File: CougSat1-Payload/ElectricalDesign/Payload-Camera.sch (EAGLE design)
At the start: 0 parts

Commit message: Added ADC
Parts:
- added C1: 4.7µF 10%, CougsInSpace-Capacitors:CAP-POL-V-4.7UF-4028
- added C2, C6, C7, C9: 100nF 10%, CougsInSpace-Capacitors:CAP-V-100NF-1608
- added C3: 10µF 10%, CougsInSpace-Capacitors:CAP-V-10UF-1608
- added C4, C5: 1µF 10%, CougsInSpace-Capacitors:CAP-V-1UF-1608
- added FB1: 1.5kΩ @ 100MHz, CougsInSpace-Coils:CHOKE-H-1.5K-1608
- added J1: CougSat Card, CougsInSpace-Boards:CIS_CARD
- added Q1: MMBTA06W, CougsInSpace-DiscreteSemi:BJT-NPN-MMBTA06W-SOT323
- added RN1: 10kΩ 5%, CougsInSpace-Resistors:RES_BUS-10-10K-3264
- added RT1, RT2, RT3, RT4, RT5, RT6, RT7, RT8: 10kΩ 5%, CougsInSpace-Resistors:THERMISTOR-V-10K-1608
- added TP1, TP2, TP3: TEST_POINT-SMD-C-1.25, CougsInSpace-Connectors:TEST_POINT-SMD-C-1.25
- added U1: AD7291, CougsInSpace-IC-Conversion:AD7291
- added U2: AD8515, CougsInSpace-IC-Amplifiers:OPAMP-1-AD8515
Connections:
- new net 3.3V_10: C9.1, FB1.1, J1POWER.PR_3.3V-10, U1.!PD!/!RST, U1.VDRIVE
- new net 3.3V_11: J1POWER.PR_3.3V-11
- new net 3.3V_12: J1POWER.PR_3.3V-12
- new net AGND: C1.C, C2.2, C3.2, C6.2, C7.2, U1.AGND, U2.V-
- new net AVDD: C1.A, C2.1, C6.1, C7.1, FB1.2, Q1.C, TP1.1, U1.VDD, U2.V+
- new net AVREF-0: C5.1, Q1.E, RN1.C, TP3.1, U2.IN-
- new net CHASSIS: J1POWER.CHASSIS
- new net DGND: C4.2, C5.2, C9.2, RT1.1, RT2.1, RT3.1, RT4.1, RT5.1, RT6.1, RT7.1, RT8.1, U1.DGND
- new net I2C_SCL: J1DATA.BUS_I2C1_SCL, U1.SCL
- new net I2C_SDA: J1DATA.BUS_I2C1_SDA, U1.SDA
- new net N$10: RN1.1, RT1.2, U1.IN7
- new net N$14: RN1.8, RT6.2, U1.IN0
- new net N$16: RN1.6, RT8.2, U1.IN2
- new net N$2: C3.1, TP2.1, U1.VREF, U2.IN+
- new net N$3: C4.1, U1.DCAP
- new net N$4: RN1.7, RT7.2, U1.IN1
- new net N$5: Q1.B, U2.OUT
- new net N$6: RN1.5, RT5.2, U1.IN3
- new net N$7: RN1.4, RT2.2, U1.IN4
- new net N$8: RN1.3, RT3.2, U1.IN5
- new net N$9: RN1.2, RT4.2, U1.IN6
- new net PGND: J1POWER.PGND
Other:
- note added: "CAD Note: Decoupling"
- note added: "Connector: Backplane"
- note added: "Page 1: Block Diagram Page 2: Power Rails Page 3: Schematic Page 4: Mechanical"
- note removed: "Connector: Backplane From EPS"
- note removed: "Connector: To Backplane"
- note removed: "Page 1: Block Diagram Page 2: Power Rails"

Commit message: Added cameras
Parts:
- removed Q1: MMBTA06W, CougsInSpace-DiscreteSemi:BJT-NPN-MMBTA06W-SOT323
- added B1, B2: ArduCam OV5642, CougsInSpace-Sensors:ARDUCAM-5MP-1.7MM-F2.8
- added D1: X100-7, CougsInSpace-Sensors:PHOTODIODE-X100-7-THD
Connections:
- net N$2 renamed ADC_VREF
- net N$3 renamed ADC_DCAP
- removed net N$5: Q1.B, U2.OUT
- new net !CS-TELEPHOTO: B1.!CS
- new net !CS-WIDE_ANGLE: B2.!CS
- new net SPI_MISO: B1.MISO, B2.MISO, J1DATA.BUS_SPI_MISO
- new net SPI_MOSI: B1.MOSI, B2.MOSI, J1DATA.BUS_SPI_MOSI
- new net SPI_SCK: B1.SCK, B2.SCK, J1DATA.BUS_SPI_SCK
- net 3.3V_11: now also B1.VCC
- net 3.3V_12: now also B2.VCC
- net AVDD: no longer Q1.C
- net AVREF-0: now also U2.OUT; no longer Q1.E
- net CHASSIS: now also B1.CHASSIS, B2.CHASSIS
- net DGND: now also B1.DGND, B2.DGND
- net I2C_SCL: now also B1.SCL, B2.SCL
- net I2C_SDA: now also B1.SDA, B2.SDA
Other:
- note added: "Page 1: Block Diagram Page 2: Power Rails Page 3: Connector/ADC/Cameras Page 4: Geiger Counter Page 4: Mechanical"
- note removed: "Page 1: Block Diagram Page 2: Power Rails Page 3: Schematic Page 4: Mechanical"

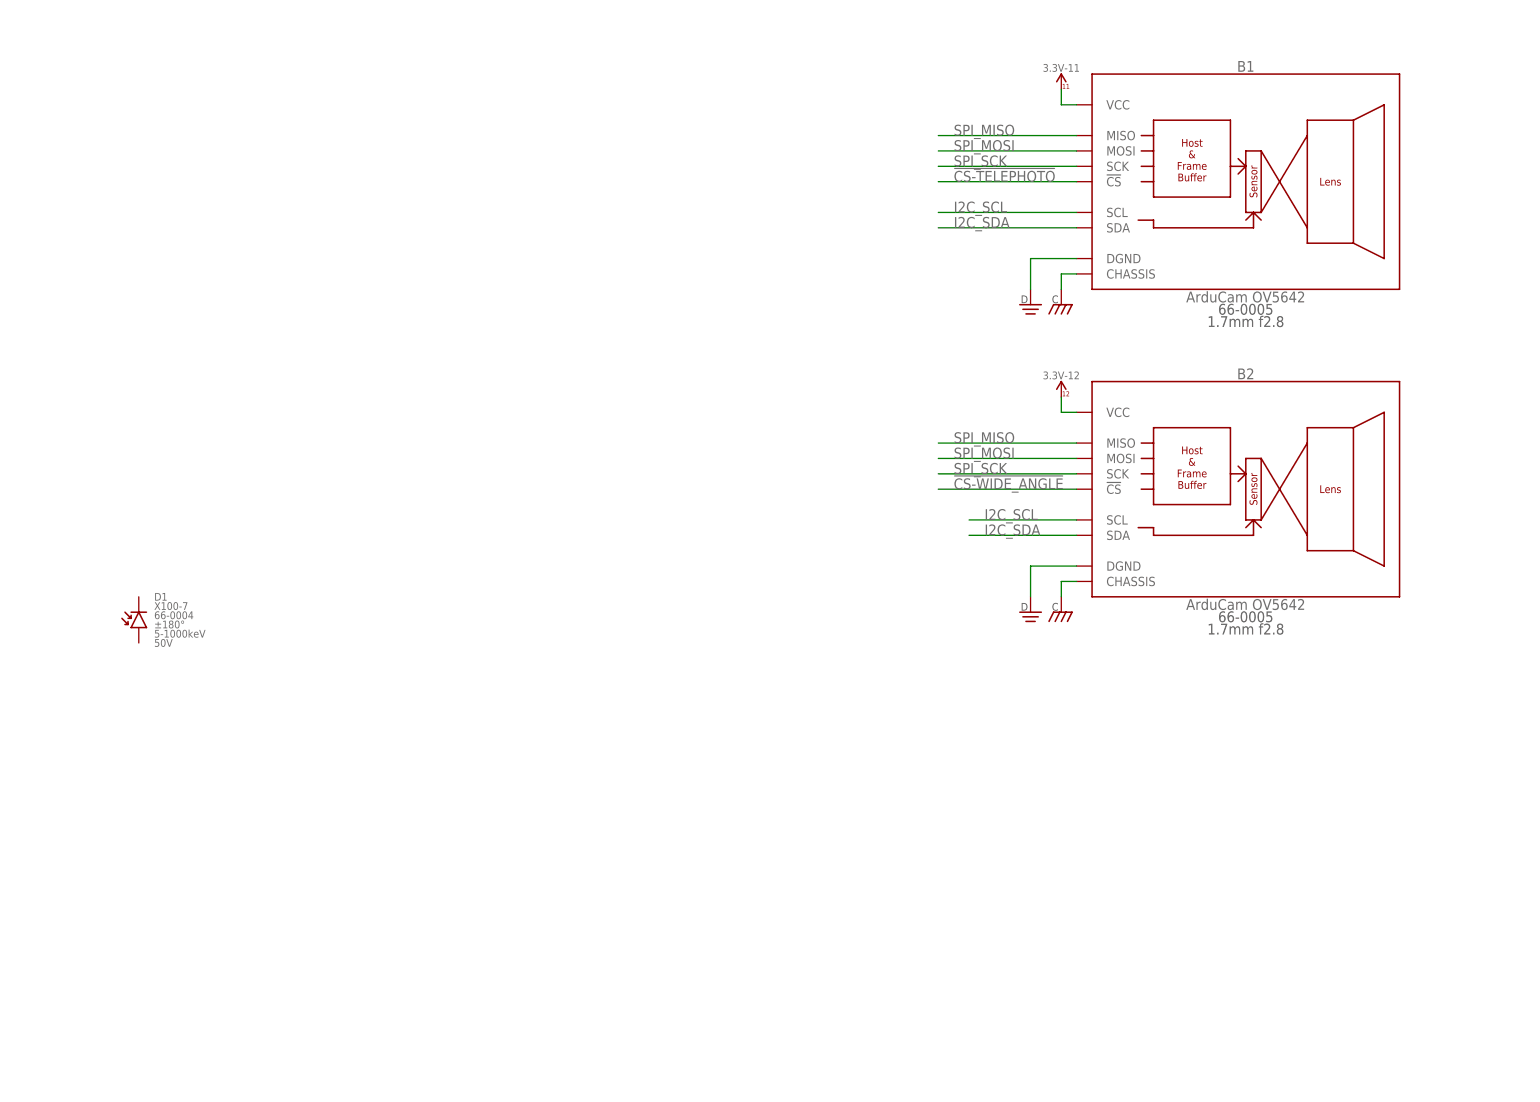
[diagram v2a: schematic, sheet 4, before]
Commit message: Added geiger counter
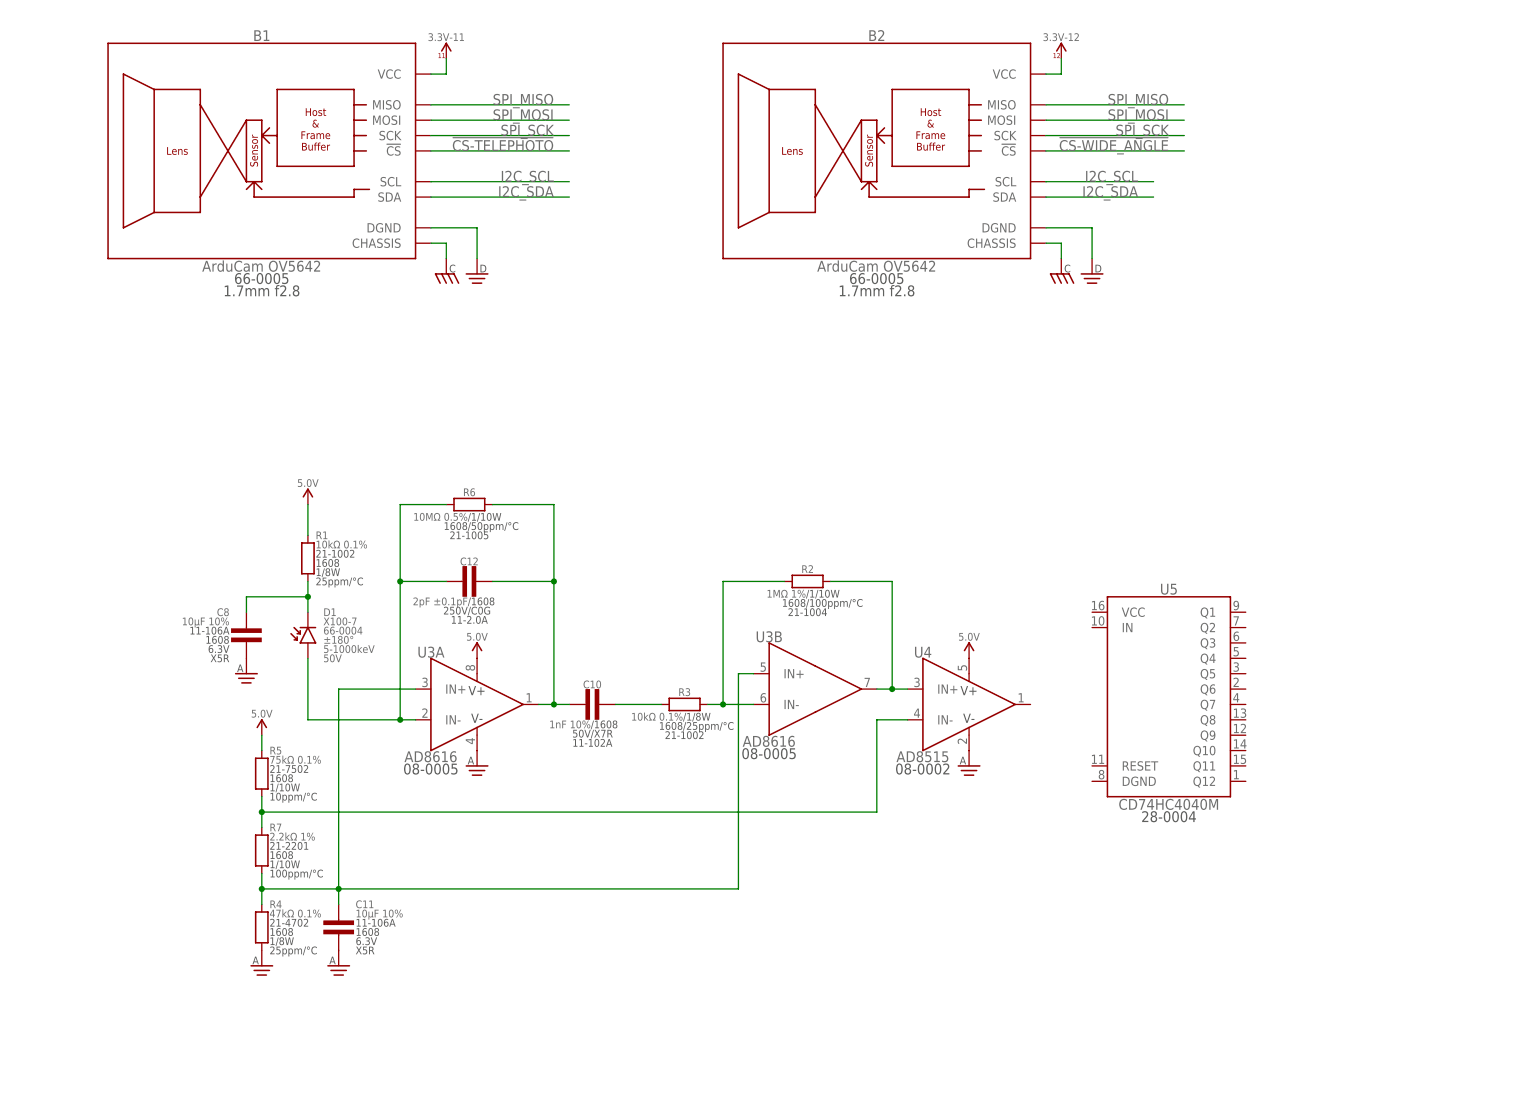
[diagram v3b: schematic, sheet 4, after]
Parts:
- added C10: 1nF 10%, CougsInSpace-Capacitors:CAP-H-1NF-1608
- added C11, C8: 10µF 10%, CougsInSpace-Capacitors:CAP-V-10UF-1608
- added C12: 2pF ±0.1pF, CougsInSpace-Capacitors:CAP-H-2PF-1608
- added R1: 10kΩ 0.1%, CougsInSpace-Resistors:RES-V-10K-1608
- added R2: 1MΩ 1%, CougsInSpace-Resistors:RES-H-1M-1608
- added R3: 10kΩ 0.1%, CougsInSpace-Resistors:RES-H-10K-1608
- added R4: 47kΩ 0.1%, CougsInSpace-Resistors:RES-V-47K-1608
- added R5: 75kΩ 0.1%, CougsInSpace-Resistors:RES-V-75K-1608
- added R6: 10MΩ 0.5%, CougsInSpace-Resistors:RES-H-10M-1608
- added R7: 2.2kΩ 1%, CougsInSpace-Resistors:RES-V-2.2K-1608
- added U3: AD8616, CougsInSpace-IC-Amplifiers:OPAMP-2-AD8616-MSOP8
- added U4: AD8515, CougsInSpace-IC-Amplifiers:OPAMP-1-AD8515
- added U5: CD74HC4040M, CougsInSpace-IC-Logic:COUNTER_BINARY-12BITSO16
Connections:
- new net 5.0V: R1.2, R5.2, U3A.V+, U4.V+
- new net N$1: C8.1, D1.C, R1.1
- new net N$11: C11.1, R4.2, R7.1, U3A.IN+, U3B.IN+
- new net N$12: C10.2, R3.1
- new net N$13: R2.1, R3.2, U3B.IN-
- new net N$15: R2.2, U3B.OUT, U4.IN+
- new net N$2: C12.1, D1.A, R6.1, U3A.IN-
- new net N$3: R5.1, R7.2, U4.IN-
- new net N$5: C10.1, C12.2, R6.2, U3A.OUT
- net AGND: now also C11.2, C8.2, R4.1, U3A.V-, U4.V-
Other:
- moved on the sheet: B1, B2, D1

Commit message: Created design document
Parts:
- added C13: 10nF 10%, CougsInSpace-Capacitors:CAP-V-10NF-1608
- added C14, C15: 10µF 10%, CougsInSpace-Capacitors:CAP-V-10UF-1608
- added U6: TPS73250, CougsInSpace-IC-Power:LDO-FB-5.0-SOT23-5
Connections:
- new net N$17: U4.OUT, U5.IN
- new net N$18: U6.EN, U6.IN
- new net N$19: C13.1, U6.FB
- net 3.3V_10: now also U5.VCC
- net 5.0V: now also C14.1, U6.OUT
- net DGND: now also U5.DGND
- net PGND: now also C13.2, C14.2, U6.PGND
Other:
- note added: "3xx>"
- note added: "3xx> 4xx>"
- note added: "4xx>"
- note added: "4xx> 4xx>"
- note added: "<3xx"
- note added: "<3xx>"
- note added: "<3xx> <4xx>"
- note added: "<4xx <4xx"
- moved on the sheet: C10, C11, C12, C3, C4, C5, C6, C7, C8, C9, D1, R1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

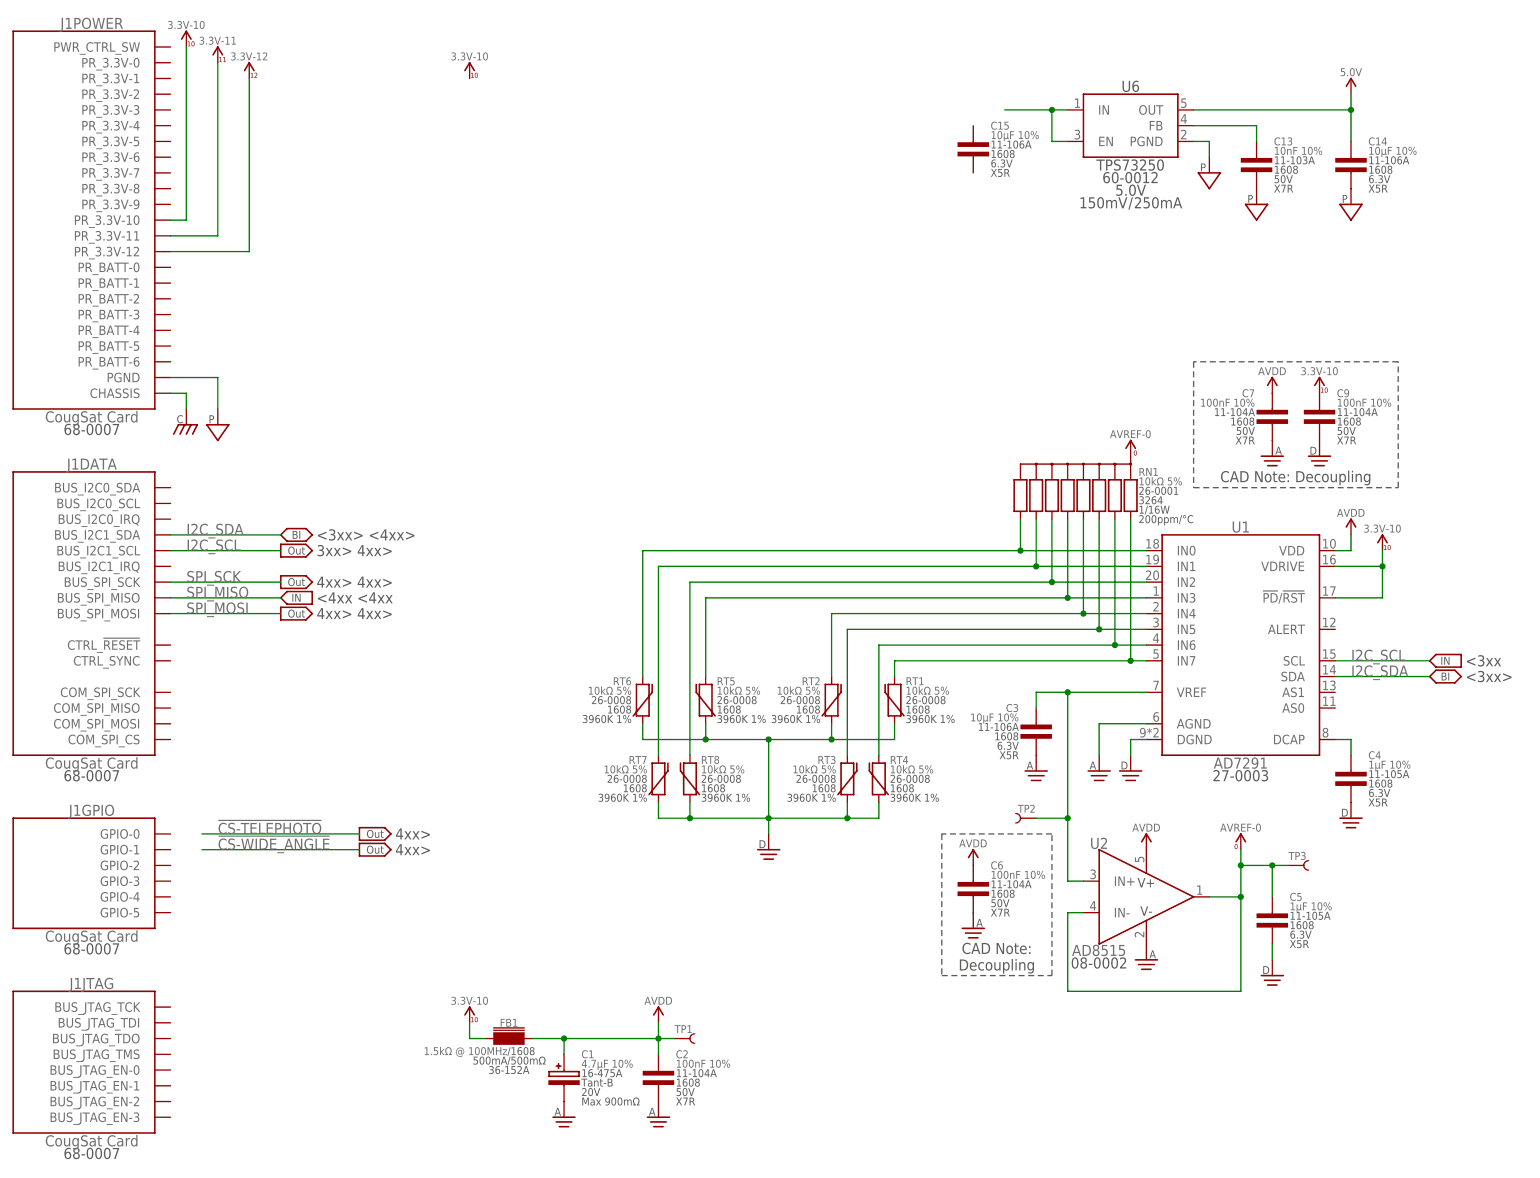
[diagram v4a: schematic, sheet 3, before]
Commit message: Added GPIO Expander
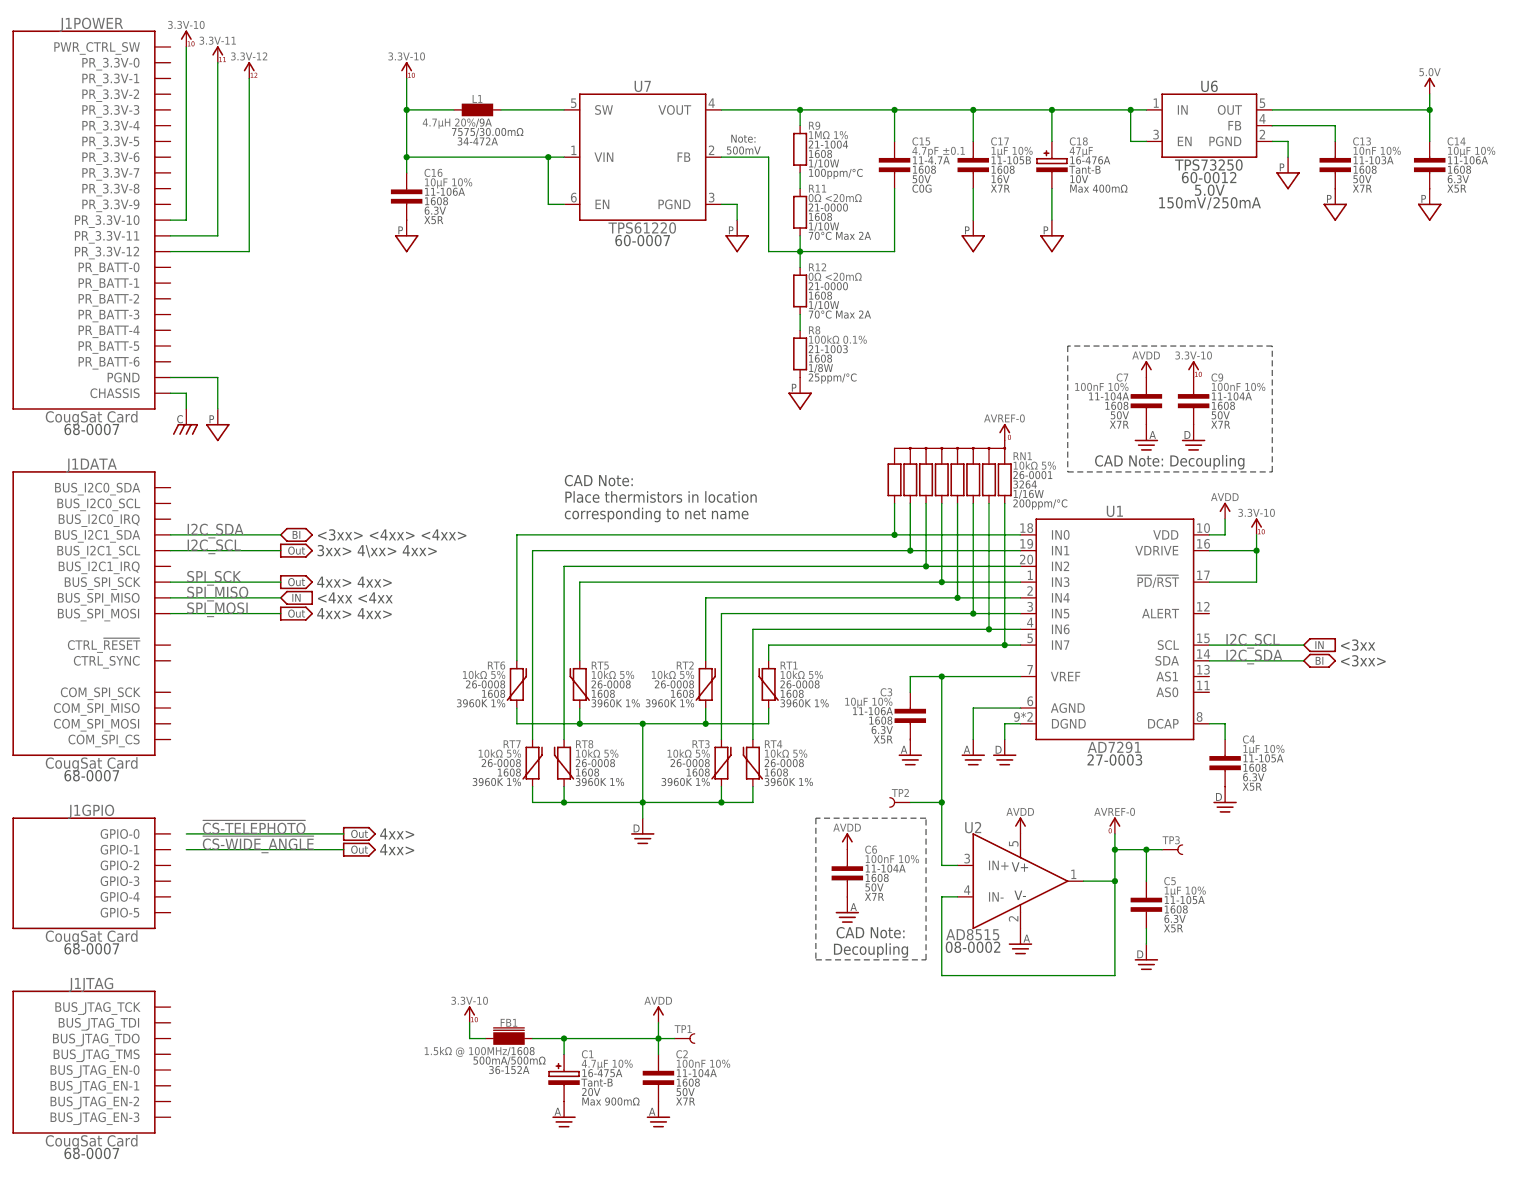
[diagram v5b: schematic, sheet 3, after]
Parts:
- added C16: 10µF 10%, CougsInSpace-Capacitors:CAP-V-10UF-1608
- added C17: 1µF 10%, CougsInSpace-Capacitors:CAP-V-1UF-B-1608
- added C18: 47µF, CougsInSpace-Capacitors:CAP-POL-V-47UF-4028
- added L1: 4.7µH 20%, CougsInSpace-Coils:INDUCTOR-H-4.7UH-7575
- added R10, R11, R12, R13: 0Ω <20mΩ, CougsInSpace-Resistors:RES-V-0-1608
- added R8: 100kΩ 0.1%, CougsInSpace-Resistors:RES-V-100K-1608
- added R9: 1MΩ 1%, CougsInSpace-Resistors:RES-V-1M-1608
- added U7: TPS61220, CougsInSpace-IC-Power:TPS61220
- added U8: TCA9535R, CougsInSpace-IC-Conversion:TCA9535R
- C15: value 10µF 10% -> 4.7pF ±0.1; device CougsInSpace-Capacitors:CAP-V-10UF-1608 -> CougsInSpace-Capacitors:CAP-V-4.7PF-1608
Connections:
- net N$19 renamed REG_FB
- new net BOOST_FB: C15.2, R11.1, R12.2, U7.FB
- new net BOOST_FB-HIGH: R11.2, R9.1
- new net BOOST_FB-LOW: R12.1, R8.2
- new net BOOST_IN: L1.2, U7.SW
- new net BOOST_OUT: C15.1, C17.1, C18.A, R9.2, U6.EN, U6.IN, U7.VOUT
- new net N$21: U5.Q1, U8.P00
- new net N$25: U5.Q2, U8.P01
- new net N$26: U5.Q3, U8.P02
- new net N$27: U5.Q4, U8.P03
- new net N$28: U5.Q5, U8.P04
- new net N$29: U5.Q6, U8.P05
- new net N$30: U5.Q7, U8.P06
- new net N$31: U5.Q8, U8.P07
- new net N$32: U5.Q9, U8.P10
- new net N$33: U5.Q10, U8.P11
- new net N$34: U5.Q11, U8.P12
- new net N$35: U5.Q12, U8.P13
- net 3.3V_10: now also C16.1, L1.1, U7.EN, U7.VIN, U8.VCC
- net AGND: now also R13.1
- net DGND: now also R10.1, U8.DGND
- net I2C_SCL: now also U8.SCL
- net I2C_SDA: now also U8.SDA
- net N$18: now also U5.RESET, U8.P14; no longer U6.EN, U6.IN
- net PGND: now also C16.2, C17.2, C18.C, R10.2, R13.2, R8.1, U7.PGND
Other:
- note added: "3xx> 4\xx> 4xx>"
- note added: "<3xx> <4xx> <4xx>"
- note added: "<4xx"
- note added: "<4xx>"
- note added: "CAD Note: Place thermistors in location corresponding to net name"
- note added: "Note: 500mV"
- note removed: "3xx> 4xx>"
- note removed: "<3xx> <4xx>"
- moved on the sheet: C10, C11, C12, C13, C14, C15, C3, C4, C5, C6, C7, C8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
